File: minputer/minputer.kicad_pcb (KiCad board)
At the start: 2 copper layers, 100 x 60 mm, 0 parts

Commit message: Assign footprints
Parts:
- added C1: 0.1u, Capacitor_THT:C_Disc_D4.3mm_W1.9mm_P5.00mm, F.Cu at (290.1, 90.1)
- added C10: 0.1u, Capacitor_THT:C_Disc_D4.3mm_W1.9mm_P5.00mm, F.Cu at (200.4, 65.1)
- added C11: 150u, Capacitor_THT:C_Radial_D8.0mm_H7.0mm_P3.50mm, F.Cu at (165.1, 81.3)
- added C12: 150u, Capacitor_THT:C_Radial_D8.0mm_H7.0mm_P3.50mm, F.Cu at (43.2, 94.0)
- added C13: 4.7u, Capacitor_THT:C_Disc_D4.3mm_W1.9mm_P5.00mm, F.Cu at (274.7, 95.6)
- added C14: 4.7u, Capacitor_THT:C_Disc_D4.3mm_W1.9mm_P5.00mm, F.Cu at (228.6, 30.5)
- added C15: 0.1u, Capacitor_THT:C_Disc_D4.3mm_W1.9mm_P5.00mm, F.Cu at (250.9, 121.3)
- added C16: 0.1u, Capacitor_THT:C_Disc_D4.3mm_W1.9mm_P5.00mm, F.Cu at (204.5, 68.6)
- added C2: 0.1u, Capacitor_THT:C_Disc_D4.3mm_W1.9mm_P5.00mm, F.Cu at (284.1, 96.4)
- added C3: 0.1u, Capacitor_THT:C_Disc_D4.3mm_W1.9mm_P5.00mm, F.Cu at (119.4, 45.7)
- added C4: 0.1u, Capacitor_THT:C_Disc_D4.3mm_W1.9mm_P5.00mm, F.Cu at (134.7, 35.6)
- added C5: 0.1u, Capacitor_THT:C_Disc_D4.3mm_W1.9mm_P5.00mm, F.Cu at (274.7, 92.2)
- added C6: 0.1u, Capacitor_THT:C_Disc_D4.3mm_W1.9mm_P5.00mm, F.Cu at (258.4, 115.7)
- added C7: 0.1u, Capacitor_THT:C_Disc_D4.3mm_W1.9mm_P5.00mm, F.Cu at (198.4, 77.3)
- added C8: 0.1u, Capacitor_THT:C_Disc_D4.3mm_W1.9mm_P5.00mm, F.Cu at (220.7, 54.2)
- added C9: 0.1u, Capacitor_THT:C_Disc_D4.3mm_W1.9mm_P5.00mm, F.Cu at (208.5, 65.1)
- added D1: D_TVS, Diode_SMD:D_0603_1608Metric_Pad1.05x0.95mm_HandSolder, F.Cu at (207.2, 76.8)
- added D10: D_TVS, Diode_SMD:D_0603_1608Metric_Pad1.05x0.95mm_HandSolder, F.Cu at (250.1, 35.6)
- added D11: D_TVS, Diode_SMD:D_0603_1608Metric_Pad1.05x0.95mm_HandSolder, F.Cu at (254.5, 33.0)
- added D12: D_TVS, Diode_SMD:D_0603_1608Metric_Pad1.05x0.95mm_HandSolder, F.Cu at (295.1, 93.2)
- added D13: D_TVS, Diode_SMD:D_0603_1608Metric_Pad1.05x0.95mm_HandSolder, F.Cu at (243.6, 39.2)
- added D14: D_TVS, Diode_SMD:D_0603_1608Metric_Pad1.05x0.95mm_HandSolder, F.Cu at (271.8, 114.3)
- added D15: D_TVS, Diode_SMD:D_0603_1608Metric_Pad1.05x0.95mm_HandSolder, F.Cu at (223.6, 50.7)
- added D16: D_TVS, Diode_SMD:D_0603_1608Metric_Pad1.05x0.95mm_HandSolder, F.Cu at (229.5, 53.3)
- added D17: D_TVS, Diode_SMD:D_0603_1608Metric_Pad1.05x0.95mm_HandSolder, F.Cu at (205.1, 71.6)
- added D18: D_TVS, Diode_SMD:D_0603_1608Metric_Pad1.05x0.95mm_HandSolder, F.Cu at (256.0, 99.5)
- added D19: D_TVS, Diode_SMD:D_0603_1608Metric_Pad1.05x0.95mm_HandSolder, F.Cu at (284.8, 99.4)
- added D2: D_TVS, Diode_SMD:D_0603_1608Metric_Pad1.05x0.95mm_HandSolder, F.Cu at (248.0, 39.2)
- added D20: D_TVS, Diode_SMD:D_0603_1608Metric_Pad1.05x0.95mm_HandSolder, F.Cu at (229.5, 55.9)
- added D21: LED, LED_THT:LED_D5.0mm, F.Cu at (213.5, 70.6)
- added D22: LED, LED_THT:LED_D5.0mm, F.Cu at (221.6, 59.7)
- added D23: D_TVS, Diode_SMD:D_0603_1608Metric_Pad1.05x0.95mm_HandSolder, F.Cu at (233.9, 51.0)
- added D24: D_TVS, Diode_SMD:D_0603_1608Metric_Pad1.05x0.95mm_HandSolder, F.Cu at (264.1, 124.0)
- added D25: D_TVS, Diode_SMD:D_0603_1608Metric_Pad1.05x0.95mm_HandSolder, F.Cu at (217.3, 64.8)
- added D26: D_TVS, Diode_SMD:D_0603_1608Metric_Pad1.05x0.95mm_HandSolder, F.Cu at (205.1, 74.2)
- added D27: D_TVS, Diode_SMD:D_0603_1608Metric_Pad1.05x0.95mm_HandSolder, F.Cu at (292.9, 95.7)
- added D28: LED, LED_THT:LED_D5.0mm, F.Cu at (234.5, 45.9)
- added D29: D_TVS, Diode_SMD:D_0603_1608Metric_Pad1.05x0.95mm_HandSolder, F.Cu at (201.2, 122.8)
- added D3: D_TVS, Diode_SMD:D_0603_1608Metric_Pad1.05x0.95mm_HandSolder, F.Cu at (280.3, 103.2)
- added D30: D_TVS, Diode_SMD:D_0603_1608Metric_Pad1.05x0.95mm_HandSolder, F.Cu at (298.9, 88.8)
- added D31: D_TVS, Diode_SMD:D_0603_1608Metric_Pad1.05x0.95mm_HandSolder, F.Cu at (274.2, 111.7)
- added D32: D_TVS, Diode_SMD:D_0603_1608Metric_Pad1.05x0.95mm_HandSolder, F.Cu at (290.7, 93.2)
- added D33: D_TVS, Diode_SMD:D_0603_1608Metric_Pad1.05x0.95mm_HandSolder, F.Cu at (289.2, 99.4)
- added D34: D_TVS, Diode_SMD:D_0603_1608Metric_Pad1.05x0.95mm_HandSolder, F.Cu at (269.8, 111.7)
- added D35: D_TVS, Diode_SMD:D_0603_1608Metric_Pad1.05x0.95mm_HandSolder, F.Cu at (243.6, 41.8)
- added D4: D_TVS, Diode_SMD:D_0603_1608Metric_Pad1.05x0.95mm_HandSolder, F.Cu at (259.7, 124.0)
- added D5: D_TVS, Diode_SMD:D_0603_1608Metric_Pad1.05x0.95mm_HandSolder, F.Cu at (233.9, 53.5)
- added D6: D_TVS, Diode_SMD:D_0603_1608Metric_Pad1.05x0.95mm_HandSolder, F.Cu at (250.1, 33.0)
- added D7: D_TVS, Diode_SMD:D_0603_1608Metric_Pad1.05x0.95mm_HandSolder, F.Cu at (284.8, 102.0)
- added D8: D_TVS, Diode_SMD:D_0603_1608Metric_Pad1.05x0.95mm_HandSolder, F.Cu at (280.3, 105.7)
- added D9: D_TVS, Diode_SMD:D_0603_1608Metric_Pad1.05x0.95mm_HandSolder, F.Cu at (228.0, 50.7)
- added J1: Conn_02x10_Odd_Even, Connector_PinHeader_2.54mm:PinHeader_2x10_P2.54mm_Vertical, F.Cu at (201.3, 96.4)
- added J2: Conn_01x03_Male, Connector_PinHeader_2.54mm:PinHeader_1x03_P2.54mm_Vertical, F.Cu at (286.2, 87.3)
- added J3: Conn_01x02_Male, Connector_PinHeader_2.54mm:PinHeader_1x02_P2.54mm_Vertical, F.Cu at (267.3, 116.3)
- added J4: Conn_02x20_Odd_Even, Connector_PinHeader_2.54mm:PinHeader_2x20_P2.54mm_Vertical, F.Cu at (31.2, 37.1)
- added J5: Conn_02x05_Odd_Even, Connector_PinHeader_2.54mm:PinHeader_2x05_P2.54mm_Vertical, F.Cu at (256.1, 85.7)
- added P1: USB_C_Plug_USB2.0, Connector_USB:USB_C_Receptacle_Amphenol_12401548E4-2A, F.Cu at (170.2, 94.0)
- added R1: 1k, Resistor_THT:R_Axial_DIN0207_L6.3mm_D2.5mm_P7.62mm_Horizontal, F.Cu at (273.4, 99.8)
- added R10: 1k, Resistor_THT:R_Axial_DIN0207_L6.3mm_D2.5mm_P7.62mm_Horizontal, F.Cu at (224.0, 37.8)
- added R11: 1k, Resistor_THT:R_Axial_DIN0207_L6.3mm_D2.5mm_P7.62mm_Horizontal, F.Cu at (189.6, 53.3)
- added R12: 1k, Resistor_THT:R_Axial_DIN0207_L6.3mm_D2.5mm_P7.62mm_Horizontal, F.Cu at (200.4, 53.3)
- added R13: 1k, Resistor_THT:R_Axial_DIN0207_L6.3mm_D2.5mm_P7.62mm_Horizontal, F.Cu at (212.2, 46.4)
- added R14: 1k, Resistor_THT:R_Axial_DIN0207_L6.3mm_D2.5mm_P7.62mm_Horizontal, F.Cu at (262.6, 99.8)
- added R15: 1k, Resistor_THT:R_Axial_DIN0207_L6.3mm_D2.5mm_P7.62mm_Horizontal, F.Cu at (82.5, 33.0)
- added R16: 1k, Resistor_THT:R_Axial_DIN0207_L6.3mm_D2.5mm_P7.62mm_Horizontal, F.Cu at (102.9, 33.0)
- added R17: 1k, Resistor_THT:R_Axial_DIN0207_L6.3mm_D2.5mm_P7.62mm_Horizontal, F.Cu at (193.7, 69.5)
- added R18: 330, Resistor_THT:R_Axial_DIN0207_L6.3mm_D2.5mm_P7.62mm_Horizontal, F.Cu at (258.4, 103.9)
- added R19: 1k, Resistor_THT:R_Axial_DIN0207_L6.3mm_D2.5mm_P7.62mm_Horizontal, F.Cu at (200.4, 57.3)
- added R2: 1k, Resistor_THT:R_Axial_DIN0207_L6.3mm_D2.5mm_P7.62mm_Horizontal, F.Cu at (193.7, 73.5)
- added R20: 1k, Resistor_THT:R_Axial_DIN0207_L6.3mm_D2.5mm_P7.62mm_Horizontal, F.Cu at (212.2, 50.5)
- added R21: 330, Resistor_THT:R_Axial_DIN0207_L6.3mm_D2.5mm_P7.62mm_Horizontal, F.Cu at (258.4, 112.0)
- added R22: 10k, Resistor_THT:R_Axial_DIN0207_L6.3mm_D2.5mm_P7.62mm_Horizontal, F.Cu at (240.1, 121.6)
- added R23: 1k, Resistor_THT:R_Axial_DIN0207_L6.3mm_D2.5mm_P7.62mm_Horizontal, F.Cu at (200.4, 61.4)
- added R24: 1k, Resistor_THT:R_Axial_DIN0207_L6.3mm_D2.5mm_P7.62mm_Horizontal, F.Cu at (258.4, 107.9)
- added R25: 330, Resistor_THT:R_Axial_DIN0207_L6.3mm_D2.5mm_P7.62mm_Horizontal, F.Cu at (41.9, 33.0)
- added R26: 22.1k, Resistor_SMD:R_0603_1608Metric_Pad0.98x0.95mm_HandSolder, F.Cu at (221.7, 64.8)
- added R27: 47.5k, Resistor_SMD:R_0603_1608Metric_Pad0.98x0.95mm_HandSolder, F.Cu at (271.8, 116.8)
- added R28: 5.1k, Resistor_SMD:R_0603_1608Metric_Pad0.98x0.95mm_HandSolder, F.Cu at (211.5, 75.7)
- added R3: 1k, Resistor_THT:R_Axial_DIN0207_L6.3mm_D2.5mm_P7.62mm_Horizontal, F.Cu at (218.6, 121.1)
- added R4: 1k, Resistor_THT:R_Axial_DIN0207_L6.3mm_D2.5mm_P7.62mm_Horizontal, F.Cu at (189.6, 65.4)
- added R5: 1k, Resistor_THT:R_Axial_DIN0207_L6.3mm_D2.5mm_P7.62mm_Horizontal, F.Cu at (229.3, 121.1)
- added R6: 1k, Resistor_THT:R_Axial_DIN0207_L6.3mm_D2.5mm_P7.62mm_Horizontal, F.Cu at (189.6, 61.4)
- added R7: 1k, Resistor_THT:R_Axial_DIN0207_L6.3mm_D2.5mm_P7.62mm_Horizontal, F.Cu at (207.7, 122.6)
- added R8: 1k, Resistor_THT:R_Axial_DIN0207_L6.3mm_D2.5mm_P7.62mm_Horizontal, F.Cu at (189.6, 57.3)
- added R9: 1k, Resistor_THT:R_Axial_DIN0207_L6.3mm_D2.5mm_P7.62mm_Horizontal, F.Cu at (62.2, 33.0)
- added SW1: SW_Push, Button_Switch_THT:SW_PUSH_6mm, F.Cu at (269.6, 103.9)
- added U1: DS1318, Package_TO_SOT_THT:TO-92L_HandSolder, F.Cu at (243.3, 35.3)
- added U10: W65C22, Package_DIP:DIP-40_W15.24mm, F.Cu at (38.1, 38.1)
- added U11: 16C2552_PLCC, Package_LCC:PLCC-44_THT-Socket, F.Cu at (127.0, 48.3)
- added U12: CP2102N-Axx-xQFN20, Package_DFN_QFN:VQFN-20-1EP_3x3mm_P0.45mm_EP1.55x1.55mm, F.Cu at (260.1, 120.1)
- added U2: 74LS138, Package_DIP:DIP-16_W7.62mm, F.Cu at (119.4, 76.2)
- added U3: W65C816, Package_DIP:DIP-40_W15.24mm, F.Cu at (58.4, 38.1)
- added U4: 74HC00, Package_DIP:DIP-14_W7.62mm, F.Cu at (106.7, 76.2)
- added U5: 74HC00, Package_DIP:DIP-14_W7.62mm, F.Cu at (132.1, 76.2)
- added U6: 28C256, Package_DIP:DIP-28_W15.24mm, F.Cu at (99.1, 38.1)
- added U7: 74HC02, Package_DIP:DIP-14_W7.62mm, F.Cu at (144.8, 76.2)
- added U8: AS6C4008-55PCN, Package_DIP:DIP-32_W15.24mm, F.Cu at (78.7, 38.1)
- added U9: 74LS573, Package_DIP:DIP-20_W7.62mm, F.Cu at (101.6, 83.8)
- added X1: CXO_DIP8, Oscillator:Oscillator_DIP-8, F.Cu at (160.0, 40.6)
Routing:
- added copper zone on In2.Cu, net GND
- added copper zone on In1.Cu, net VDD
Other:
- board size 100 x 60 mm -> 150 x 80 mm
- copper layers 2 -> 4

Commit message: Component placement and TVS routing finished
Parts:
- removed R10: 1k, Resistor_THT:R_Axial_DIN0207_L6.3mm_D2.5mm_P7.62mm_Horizontal
- added D36: D_TVS, Diode_SMD:D_0603_1608Metric_Pad1.05x0.95mm_HandSolder, B.Cu at (49.5, 103.5)
- added D37: D_TVS, Diode_SMD:D_0603_1608Metric_Pad1.05x0.95mm_HandSolder, B.Cu at (52.1, 103.5)
- added D38: D_TVS, Diode_SMD:D_0603_1608Metric_Pad1.05x0.95mm_HandSolder, B.Cu at (54.6, 103.5)
- added D39: D_TVS, Diode_SMD:D_0603_1608Metric_Pad1.05x0.95mm_HandSolder, B.Cu at (57.1, 103.5)
- added D40: D_TVS, Diode_SMD:D_0603_1608Metric_Pad1.05x0.95mm_HandSolder, B.Cu at (59.7, 103.5)
- added D41: D_TVS, Diode_SMD:D_0603_1608Metric_Pad1.05x0.95mm_HandSolder, B.Cu at (62.2, 103.5)
- added D42: D_TVS, Diode_SMD:D_0603_1608Metric_Pad1.05x0.95mm_HandSolder, B.Cu at (64.8, 103.5)
- added D43: D_TVS, Diode_SMD:D_0603_1608Metric_Pad1.05x0.95mm_HandSolder, B.Cu at (67.3, 103.5)
- added D44: D_TVS, Diode_SMD:D_0603_1608Metric_Pad1.05x0.95mm_HandSolder, B.Cu at (69.8, 103.5)
- added D45: D_TVS, Diode_SMD:D_0603_1608Metric_Pad1.05x0.95mm_HandSolder, B.Cu at (72.4, 103.5)
- added D46: D_TVS, Diode_SMD:D_0603_1608Metric_Pad1.05x0.95mm_HandSolder, B.Cu at (54.6, 112.4)
- added D47: D_TVS, Diode_SMD:D_0603_1608Metric_Pad1.05x0.95mm_HandSolder, B.Cu at (57.1, 112.4)
- added D48: D_TVS, Diode_SMD:D_0603_1608Metric_Pad1.05x0.95mm_HandSolder, B.Cu at (59.7, 112.4)
- added D49: D_TVS, Diode_SMD:D_0603_1608Metric_Pad1.05x0.95mm_HandSolder, B.Cu at (62.2, 112.4)
- added D50: D_TVS, Diode_SMD:D_0603_1608Metric_Pad1.05x0.95mm_HandSolder, B.Cu at (64.8, 112.4)
- added D51: D_TVS, Diode_SMD:D_0603_1608Metric_Pad1.05x0.95mm_HandSolder, B.Cu at (67.3, 112.4)
- added D52: D_TVS, Diode_SMD:D_0603_1608Metric_Pad1.05x0.95mm_HandSolder, B.Cu at (69.8, 112.4)
- added H1: MountingHole_Pad, MountingHole:MountingHole_4.3mm_M4_DIN965_Pad, F.Cu at (167.5, 32.5)
- added H2: MountingHole_Pad, MountingHole:MountingHole_4.3mm_M4_DIN965_Pad, F.Cu at (167.5, 107.0)
- added H3: MountingHole_Pad, MountingHole:MountingHole_4.3mm_M4_DIN965_Pad, F.Cu at (32.5, 107.0)
- added H4: MountingHole_Pad, MountingHole:MountingHole_4.3mm_M4_DIN965_Pad, F.Cu at (32.5, 32.5)
- C13, C14, C15, C16: footprint Capacitor_THT:C_Disc_D4.3mm_W1.9mm_P5.00mm -> Capacitor_SMD:C_0603_1608Metric_Pad1.08x0.95mm_HandSolder
- D1, D10, D11, D12, D13, D14, D15, D16, D17, D18, D19, D2, D20, D23, D24, D25, D26, D27, D29, D3, D30, D31, D32, D4, D5, D6, D7, D8, D9: moved to B.Cu
- moved D12 259.4 mm to (36.8, 69.8), turned to 180 degrees
- moved D7 253.4 mm to (36.8, 49.5), turned to 180 degrees
- moved D8 250.5 mm to (36.8, 47.0), turned to 180 degrees
- moved D19 248.2 mm to (36.8, 87.6), turned to 180 degrees
- moved D3 247.4 mm to (36.8, 59.7), turned to 180 degrees
- moved D14 238.3 mm to (36.8, 74.9), turned to 180 degrees
- moved D4 232.7 mm to (36.8, 57.1), turned to 180 degrees
- moved C1 231.1 mm to (64.8, 38.7)
- moved D11 220.3 mm to (36.8, 67.3), turned to 180 degrees
- moved D18 219.7 mm to (36.8, 85.1), turned to 180 degrees
- moved D6 214.1 mm to (36.8, 52.1), turned to 180 degrees
- moved D10 213.4 mm to (36.8, 41.9), turned to 180 degrees
- moved D2 212.4 mm to (36.8, 62.2), turned to 180 degrees
- moved J3 210.8 mm to (57.1, 99.1), turned to -90 degrees
- moved D13 209.4 mm to (36.8, 72.4), turned to 180 degrees
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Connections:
- U9 pad 1: Net-(R10-Pad1) -> GND
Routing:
- net /PHI2: track 0.00 -> 202.8 mm, vias 0 -> 5
- net /IRQB: track 0.00 -> 135.9 mm, vias 0 -> 1
- net GND: track 0.00 -> 121.4 mm, vias 0 -> 24
- net /RESB: track 0.00 -> 87.2 mm, vias 0 -> 3
- net /RWB: track 0.00 -> 78.8 mm, vias 0 -> 3
- net /VIACSB: track 0.00 -> 77.1 mm, vias 0 -> 1
- net /IO.CA1: track 0.00 -> 76.6 mm, vias 0 -> 1
- net /IO.CA2: track 0.00 -> 67.5 mm, vias 0 -> 2
- net /NMIB: track 0.00 -> 66.1 mm, vias 0 -> 3
- net Net-(D24-Pad1): track 0.00 -> 40.6 mm, vias 0 -> 1
- net Net-(D27-Pad1): track 0.00 -> 34.5 mm, vias 0 -> 2
- net Net-(D21-Pad2): track 0.00 -> 34.3 mm
- net Net-(D23-Pad1): track 0.00 -> 32.6 mm, vias 0 -> 1
- net Net-(D31-Pad1): track 0.00 -> 30.6 mm, vias 0 -> 1
- net Net-(U11-Pad11): track 0.00 -> 29.0 mm, vias 0 -> 1
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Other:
- board size 150 x 80 mm -> 150 x 90 mm

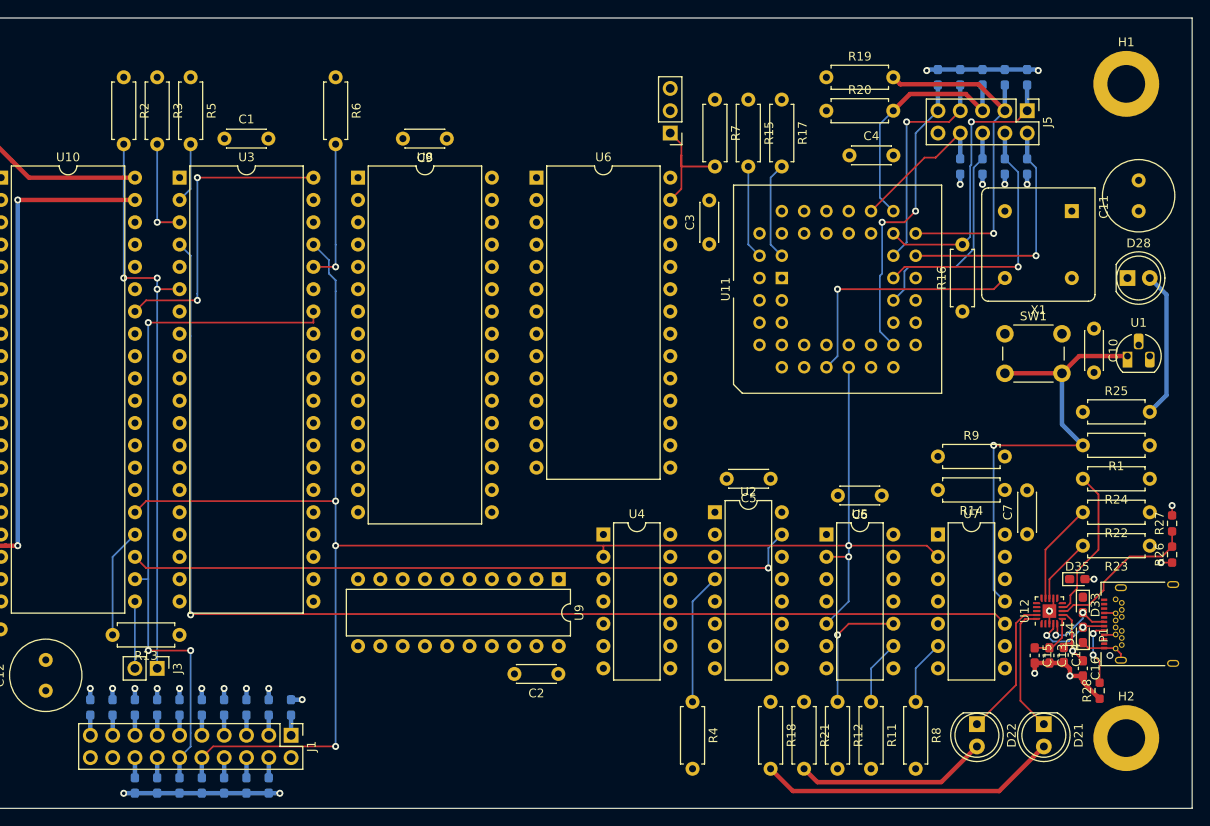
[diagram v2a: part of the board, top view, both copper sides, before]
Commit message: Remove extra 7400
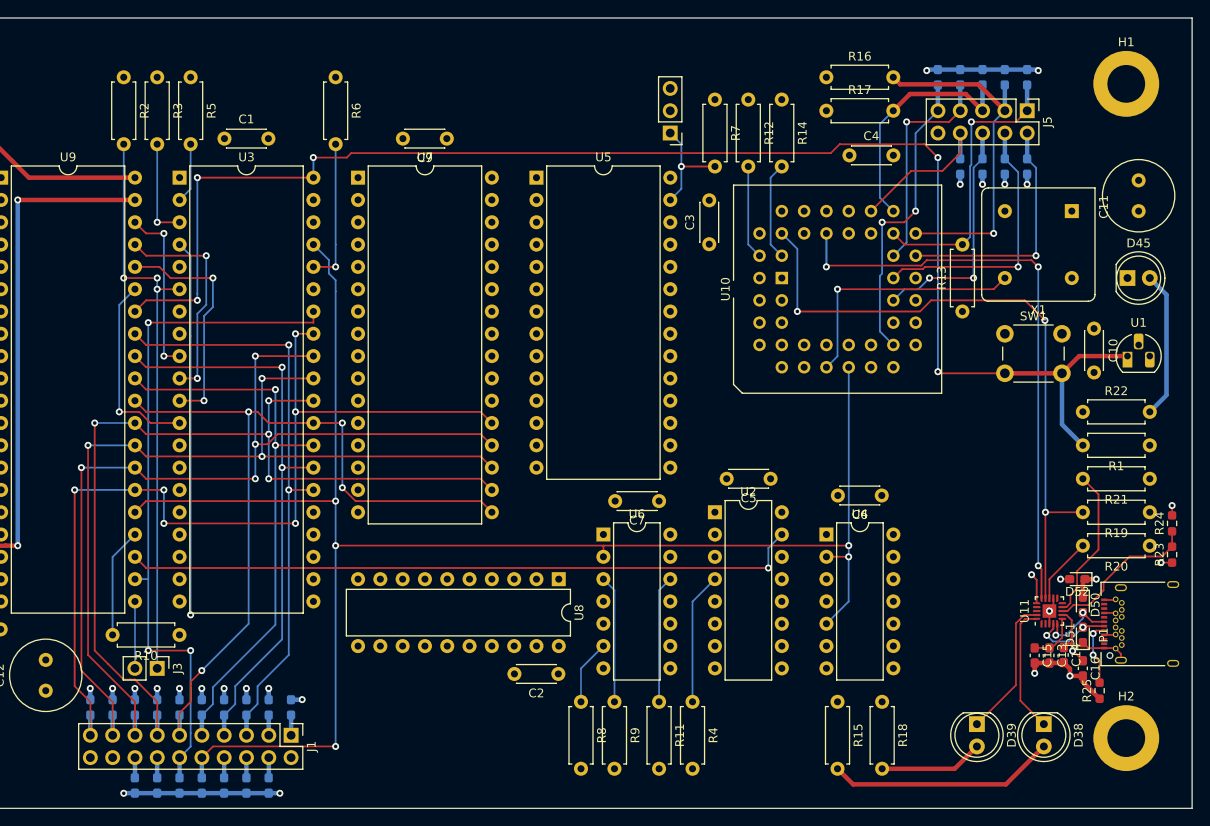
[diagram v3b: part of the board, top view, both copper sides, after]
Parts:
- removed the R11 at (138.4, 102.9)
- removed the R12 at (134.6, 102.9)
- removed the U4 at (108.0, 83.8)
- moved R9 46.2 mm to (109.2, 102.9), turned to -90 degrees
- moved R11 46.2 mm to (114.3, 102.9), turned to -90 degrees
- moved C7 42.1 mm to (114.3, 80.0), turned to 180 degrees
- moved R8 38.1 mm to (105.4, 102.9)
- moved U6 38.1 mm to (108.0, 83.8)
- moved R18 8.89 mm to (139.7, 102.9)
- moved R15 7.62 mm to (134.6, 102.9)
- turned D52 to 180 degrees
- renumbered D36 to D1, D45 to D10, D46 to D11, D47 to D12, D48 to D13, D49 to D14, D50 to D15, D51 to D16, D52 to D17, D1 to D18, D2 to D19, D37 to D2, D3 to D20, D4 to D21, D5 to D22, D6 to D23, D7 to D24, D8 to D25, D9 to D26, D10 to D27, D11 to D28, D12 to D29, D38 to D3, D13 to D30, D14 to D31, D15 to D32, D16 to D33, D17 to D34, D18 to D35, D19 to D36, D20 to D37, D21 to D38, D22 to D39, D39 to D4, D23 to D40, D24 to D41, D25 to D42, D26 to D43, D27 to D44, D28 to D45, D29 to D46, D30 to D47, D31 to D48, D32 to D49, D40 to D5, D33 to D50, D34 to D51, D35 to D52, D41 to D6, D42 to D7, D43 to D8, D44 to D9, R13 to R10, R14 to R11, R15 to R12, R16 to R13, R17 to R14, R18 to R15, R19 to R16, R20 to R17, R21 to R18, R22 to R19, R23 to R20, R24 to R21, R25 to R22, R26 to R23, R27 to R24, R28 to R25, U11 to U10, U12 to U11, U5 to U4, U6 to U5, U7 to U6, U8 to U7, U9 to U8, U10 to U9
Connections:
- D1 pad 2: /D0 -> /D7
- D2 pad 2: /D1 -> /D6
- D3 pad 2: /D2 -> /D5
- D4 pad 2: /D3 -> /D4
- D5 pad 2: /D4 -> /D3
- D6 pad 2: /D5 -> /D2
- D7 pad 2: /D6 -> /D1
- D8 pad 2: /D7 -> /D0
- J1 pad 11: /D4 -> /D3
- J1 pad 13: /D3 -> /D4
- J1 pad 15: /D2 -> /D5
- J1 pad 17: /D1 -> /D6
- J1 pad 19: /D0 -> /D7
- J1 pad 5: /D7 -> /D0
- J1 pad 7: /D6 -> /D1
- J1 pad 9: /D5 -> /D2
- U4 pad 10: Net-(R12-Pad1) -> /PHI2
- U4 pad 8: unconnected-(U5-Pad8) -> /~{WE}
- U4 pad 9: Net-(R11-Pad1) (its old number) -> /RBW
- U7 pad 13: /D7 -> /D0
- U7 pad 14: /D6 -> /D1
- U7 pad 15: /D5 -> /D2
- U7 pad 17: /D4 -> /D3
- U7 pad 18: /D3 -> /D4
- U7 pad 19: /D2 -> /D5
- U7 pad 20: /D1 -> /D6
- U7 pad 21: /D0 -> /D7
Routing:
- net /D7: track 2.30 -> 106.5 mm, vias 0 -> 6
- net /D6: track 2.30 -> 103.1 mm, vias 0 -> 4
- net /D4: track 2.30 -> 101.8 mm, vias 0 -> 4
- net /D5: track 2.30 -> 99.3 mm, vias 0 -> 3
- net /IRQB: track 135.9 -> 42.7 mm
- net /D3: track 2.30 -> 92.6 mm, vias 0 -> 4
- net /RESB: track 87.2 -> 165.5 mm, vias 3 -> 5
- net Net-(U10-Pad36): track 0.00 -> 66.5 mm, vias 0 -> 3
- net /D0: track 2.30 -> 67.3 mm, vias 0 -> 2
- net Net-(R19-Pad2): track 11.6 -> 75.2 mm, vias 0 -> 3
- net /D1: track 2.30 -> 65.5 mm, vias 0 -> 2
- net /D2: track 2.30 -> 63.7 mm, vias 0 -> 2
- net /A2: track 2.30 -> 28.9 mm, vias 0 -> 2
- net /A1: track 2.30 -> 27.4 mm, vias 0 -> 2
- net /A3: track 2.30 -> 24.4 mm, vias 0 -> 1
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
